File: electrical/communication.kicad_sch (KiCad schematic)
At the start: 13 parts

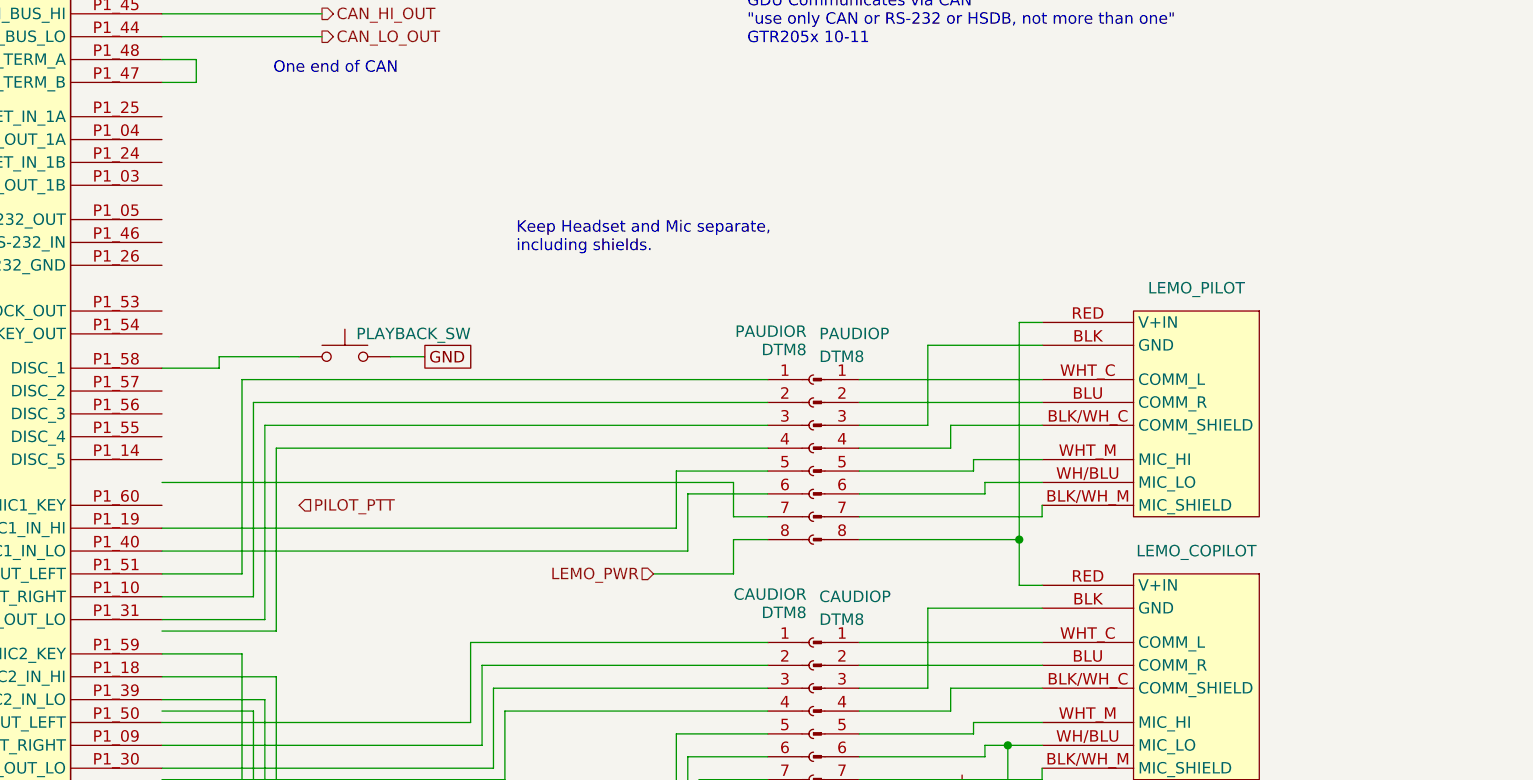
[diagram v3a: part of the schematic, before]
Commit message: Changed Lemo power to run separately. Also changed to run ground for LEMO.
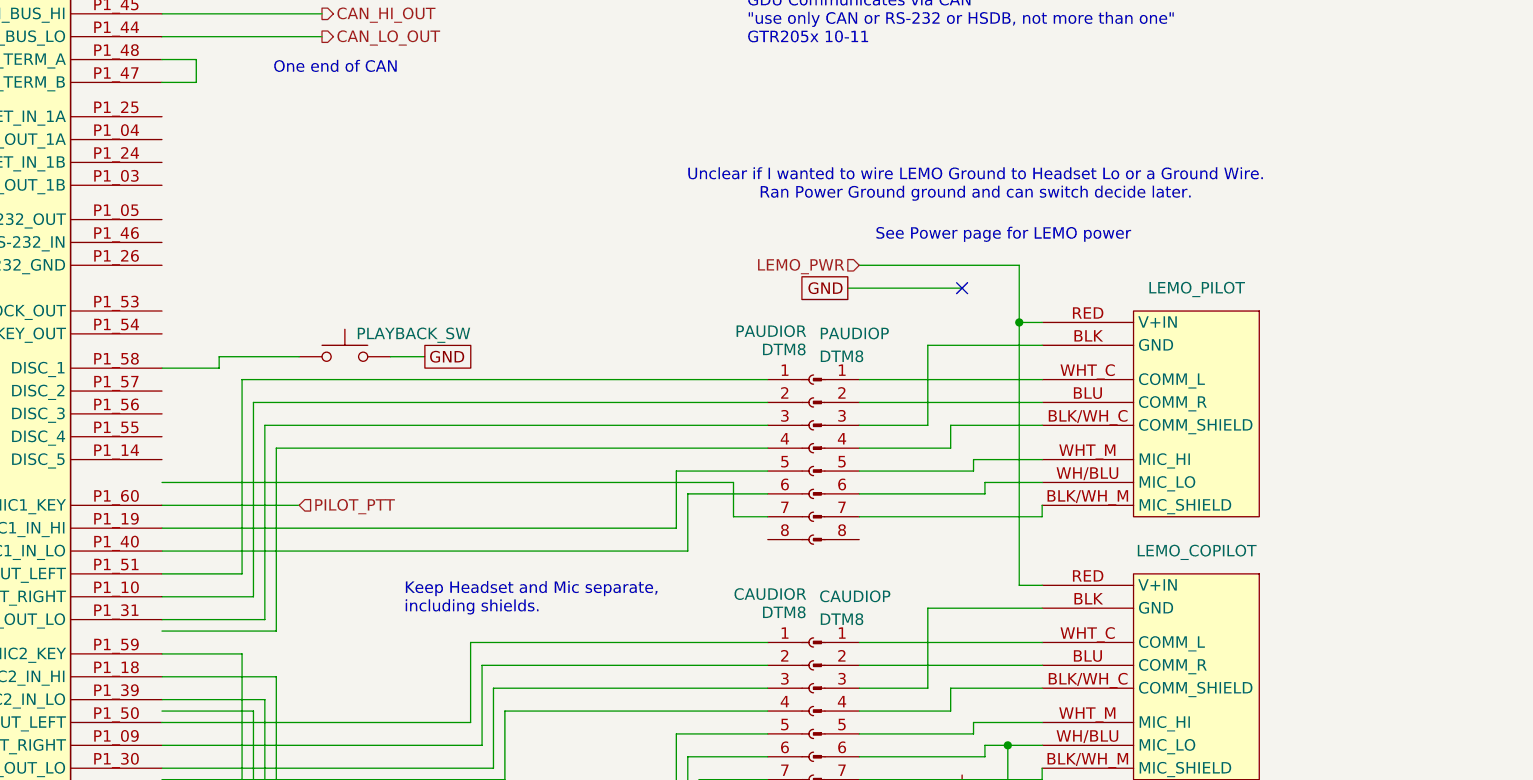
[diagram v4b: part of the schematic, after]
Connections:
- net LEMO_PWR: now also LEMO_COPILOT.RED (V+IN), LEMO_PILOT.RED (V+IN); no longer PAUDIOR.8 (Pin_8)
- net PILOT_PTT: now also GTR_205x.P1_60 (MIC1_KEY)
- now unconnected: PAUDIOP.8 (Pin_8)
- no-connect marks 2 -> 3
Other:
- note added: "See Power page for LEMO power"
- note added: "Unclear if I wanted to wire LEMO Ground to Headset Lo or a Ground Wire. Ran Power Ground ground and can switch decide later."

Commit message: Cleaned up ground vs shield markings.
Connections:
- net GNDS: now reaches PAUDIOR.4 (Pin_4)
- net GNDS: now also CAUDIOR.4 (Pin_4), CAUDIOR.7 (Pin_7), PAUDIOR.7 (Pin_7)

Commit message: Added lighting bus
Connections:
- net LIGHTS_HI: now reaches GTR_205x.P1_17 (LIGHTING_BUS_HI)
- no-connect marks 3 -> 4
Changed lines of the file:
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@@
 	(title_block
 		(title "Communication")
-		(date "2025-10-12")
-		(rev "1.1.9")
+		(date "2025-10-19")
+		(rev "1.1.15")
 		(company "N78HR")
 	)
@@
 		(at 149.86 86.36)
 	)
+	(no_connect
+		(at 60.96 38.1)
+	)
 	(wire
 		(pts
@@
 			(width 0)
 			(type dash)
+		)
+	)
+	(wire
+		(pts
+			(xy 60.96 35.56) (xy 74.93 35.56)
+		)
+		(stroke
+			(width 0)
+			(type default)
 		)
 	)
@@
 		)
 	)
+	(hierarchical_label "LIGHTS_HI"
+		(shape input)
+		(at 74.93 35.56 0)
+		(effects
+			(font
+				(size 1.27 1.27)
+			)
+			(justify left)
+		)
+	)

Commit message: Corrected all rececptacle/plug polarity and naming.
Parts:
- CAUD: renamed from CAUDIOP; value DTM8 -> DTM8R
- CAUD: renamed from CAUDIOR; value DTM8 -> DTM8P
- PAUD: renamed from PAUDIOR; value DTM8 -> DTM8P
- PAUD: renamed from PAUDIOP; value DTM8 -> DTM8R
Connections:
- net GNDS: now also CAUD.4 (Pin_4), CAUD.7 (Pin_7), PAUD.4 (Pin_4), PAUD.7 (Pin_7); no longer CAUD.4 (Pin_4), CAUD.7 (Pin_7), PAUD.4 (Pin_4), PAUD.7 (Pin_7)
- net at CAUD.1 (Pin_1): now also GTR_205x.P1_50 (HEADSET2_OUT_LEFT); no longer LEMO_COPILOT.WHT_C (COMM_L)
- net at CAUD.2 (Pin_2): now also GTR_205x.P1_09 (HEADSET2_OUT_RIGHT); no longer LEMO_COPILOT.BLU (COMM_R)
- net at CAUD.3 (Pin_3): now also GTR_205x.P1_30 (HEADSET2_OUT_LO); no longer LEMO_COPILOT.BLK (GND)
- net at LEMO_COPILOT.BLK/WH_C (COMM_SHIELD): now also CAUD.4 (Pin_4); no longer CAUD.4 (Pin_4)
- net at CAUD.5 (Pin_5): now also GTR_205x.P1_18 (MIC2_IN_HI); no longer LEMO_COPILOT.WHT_M (MIC_HI)
- net at COPILOT_PTT_SW.2, LEMO_COPILOT.WH/BLU (MIC_LO): now also CAUD.6 (Pin_6); no longer CAUD.6 (Pin_6)
- net at LEMO_COPILOT.BLK/WH_M (MIC_SHIELD): now also CAUD.7 (Pin_7); no longer CAUD.7 (Pin_7)
- net at CAUD.8 (Pin_8): now also GTR_205x.P1_59 (MIC2_KEY); no longer COPILOT_PTT_SW.1
- net at PAUD.1 (Pin_1): now also LEMO_PILOT.WHT_C (COMM_L); no longer GTR_205x.P1_51 (HEADSET1_OUT_LEFT)
- net at PAUD.2 (Pin_2): now also LEMO_PILOT.BLU (COMM_R); no longer GTR_205x.P1_10 (HEADSET1_OUT_RIGHT)
- net at PAUD.3 (Pin_3): now also LEMO_PILOT.BLK (GND); no longer GTR_205x.P1_31 (HEADSET1_OUT_LO)
- net at PAUD.5 (Pin_5): now also LEMO_PILOT.WHT_M (MIC_HI); no longer GTR_205x.P1_19 (MIC1_IN_HI)
- net at PAUD.6 (Pin_6): now also LEMO_PILOT.WH/BLU (MIC_LO); no longer GTR_205x.P1_40 (MIC1_IN_LO)
- net at PAUD.3 (Pin_3): now also GTR_205x.P1_31 (HEADSET1_OUT_LO); no longer LEMO_PILOT.BLK (GND)
- net at LEMO_PILOT.BLK/WH_C (COMM_SHIELD): now also PAUD.4 (Pin_4); no longer PAUD.4 (Pin_4)
- net at LEMO_PILOT.BLK/WH_M (MIC_SHIELD): now also PAUD.7 (Pin_7); no longer PAUD.7 (Pin_7)
- net at PAUD.2 (Pin_2): now also GTR_205x.P1_10 (HEADSET1_OUT_RIGHT); no longer LEMO_PILOT.BLU (COMM_R)
- net at PAUD.6 (Pin_6): now also GTR_205x.P1_40 (MIC1_IN_LO); no longer LEMO_PILOT.WH/BLU (MIC_LO)
- net at PAUD.1 (Pin_1): now also GTR_205x.P1_51 (HEADSET1_OUT_LEFT); no longer LEMO_PILOT.WHT_C (COMM_L)
- net at PAUD.5 (Pin_5): now also GTR_205x.P1_19 (MIC1_IN_HI); no longer LEMO_PILOT.WHT_M (MIC_HI)
- net at CAUD.1 (Pin_1): now also LEMO_COPILOT.WHT_C (COMM_L); no longer GTR_205x.P1_50 (HEADSET2_OUT_LEFT)
- net at CAUD.2 (Pin_2): now also LEMO_COPILOT.BLU (COMM_R); no longer GTR_205x.P1_09 (HEADSET2_OUT_RIGHT)
- net at CAUD.3 (Pin_3): now also LEMO_COPILOT.BLK (GND); no longer GTR_205x.P1_30 (HEADSET2_OUT_LO)
- net at CAUD.5 (Pin_5): now also LEMO_COPILOT.WHT_M (MIC_HI); no longer GTR_205x.P1_18 (MIC2_IN_HI)
- net at GTR_205x.P1_39 (MIC2_IN_LO): now also CAUD.6 (Pin_6); no longer CAUD.6 (Pin_6)
- net at CAUD.8 (Pin_8): now also COPILOT_PTT_SW.1; no longer GTR_205x.P1_59 (MIC2_KEY)
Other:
- moved on the sheet: CAUD, PAUD

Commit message: Added shielding and wire colors and corrections.
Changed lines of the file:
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@@
 	(title_block
 		(title "Communication")
-		(date "2025-11-03")
-		(rev "1.2.2")
+		(date "2025-11-12")
+		(rev "1.2.5")
 		(company "N78HR")
 	)
@@
 	(wire
 		(pts
-			(xy 60.96 107.95) (xy 124.46 107.95)
+			(xy 59.69 116.84) (xy 120.65 116.84)
 		)
 		(stroke
@@
 	(wire
 		(pts
+			(xy 60.96 59.69) (xy 78.74 59.69)
+		)
+		(stroke
+			(width 0)
+			(type dash)
+		)
+	)
+	(wire
+		(pts
 			(xy 156.21 119.38) (xy 158.75 119.38)
 		)
@@
 	(wire
 		(pts
-			(xy 124.46 107.95) (xy 124.46 111.76)
+			(xy 120.65 116.84) (xy 120.65 111.76)
 		)
 		(stroke
@@
 	(wire
 		(pts
-			(xy 124.46 111.76) (xy 128.27 111.76)
+			(xy 120.65 111.76) (xy 128.27 111.76)
 		)
 		(stroke
@@
 			(width 0)
 			(type dash)
+		)
+	)
+	(label "White"
+		(at 60.96 58.42 0)
+		(effects
+			(font
+				(size 1.27 1.27)
+			)
+			(justify left bottom)
+		)
+	)
+	(label "White{slash}Blue"
+		(at 60.96 55.88 0)
+		(effects
+			(font
+				(size 1.27 1.27)
+			)
+			(justify left bottom)
 		)
 	)
@@
 		)
 	)
-	(global_label "SHIELD"
-		(shape passive)
-		(at 88.9 82.55 180)
-		(fields_autoplaced yes)
-		(effects
-			(font
-				(size 1.27 1.27)
-			)
-			(justify right)
-		)
-		(property "Intersheetrefs" "${INTERSHEET_REFS}"
-			(at 80.4342 82.55 0)
-			(effects
-				(font
-					(size 1.27 1.27)
-				)
-				(justify right)
-				(hide yes)
-			)
-		)
-	)
 	(global_label "GND"
 		(shape passive)
@@
 	(symbol
 		(lib_id "power:GNDS")
-		(at 60.96 107.95 270)
+		(at 59.69 116.84 270)
 		(unit 1)
 		(exclude_from_sim no)
@@
 		(fields_autoplaced yes)
 		(property "Reference" "#PWR09"
-			(at 54.61 107.95 0)
+			(at 53.34 116.84 0)
 			(effects
 				(font
@@
 		)
 		(property "Value" "GNDS"
-			(at 55.88 107.95 0)
+			(at 54.61 116.84 0)
 			(effects
 				(font
@@
 		)
 		(property "Footprint" ""
-			(at 60.96 107.95 0)
+			(at 59.69 116.84 0)
 			(effects
 				(font
@@
 		)
 		(property "Datasheet" ""
-			(at 60.96 107.95 0)
+			(at 59.69 116.84 0)
 			(effects
 				(font
@@
 		)
 		(property "Description" "Power symbol creates a global label with name \"GNDS\" , signal ground"
-			(at 60.96 107.95 0)
+			(at 59.69 116.84 0)
 			(effects
 				(font
@@
 					(unit 1)
 				)
+			)
+		)
+	)
+	(symbol
+		(lib_id "power:GNDS")
+		(at 60.96 59.69 270)
+		(unit 1)
+		(exclude_from_sim no)
+		(in_bom yes)
+		(on_board yes)
+		(dnp no)
+		(fields_autoplaced yes)
+		(property "Reference" "#PWR049"
+			(at 54.61 59.69 0)
+			(effects
+				(font
+					(size 1.27 1.27)
+				)
+				(hide yes)
+			)
+		)
+		(property "Value" "GNDS"
+			(at 55.88 59.69 0)
+			(effects
+				(font
+					(size 1.27 1.27)
+				)
+				(hide yes)
+			)
+		)
+		(property "Footprint" ""
+			(at 60.96 59.69 0)
+			(effects
+				(font
+					(size 1.27 1.27)
+				)
+				(hide yes)
+			)
+		)
+		(property "Datasheet" ""
+			(at 60.96 59.69 0)
+			(effects
+				(font
+					(size 1.27 1.27)
+				)
+				(hide yes)
+			)
+		)
+		(property "Description" "Power symbol creates a global label with name \"GNDS\" , signal ground"
+			(at 60.96 59.69 0)
+			(effects
+				(font
+					(size 1.27 1.27)
+				)
+				(hide yes)
+			)
+		)
+		(pin "1"
+		)
+		(instances
+			(project "electrical"
+				(path "/e8ec215a-dbe2-4eba-a577-e50a0a128049/facdf550-4f2c-4387-974e-24c6900d900d"
+					(reference "#PWR049")
+					(unit 1)
+				)
